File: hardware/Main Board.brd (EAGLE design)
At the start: 57.1 x 76.2 mm, 52 parts, among them Q1 CSD87313DMS, Q2 CSD16406Q3, U1 BQ24210, U2 BQ29733DSER, U3 LP38693MPX-ADJ/NOPB, U4 ESP-WROOM-02D, U5 INA219AID, U6 TC78H630FNG/TSSOP16, U7 LT1716

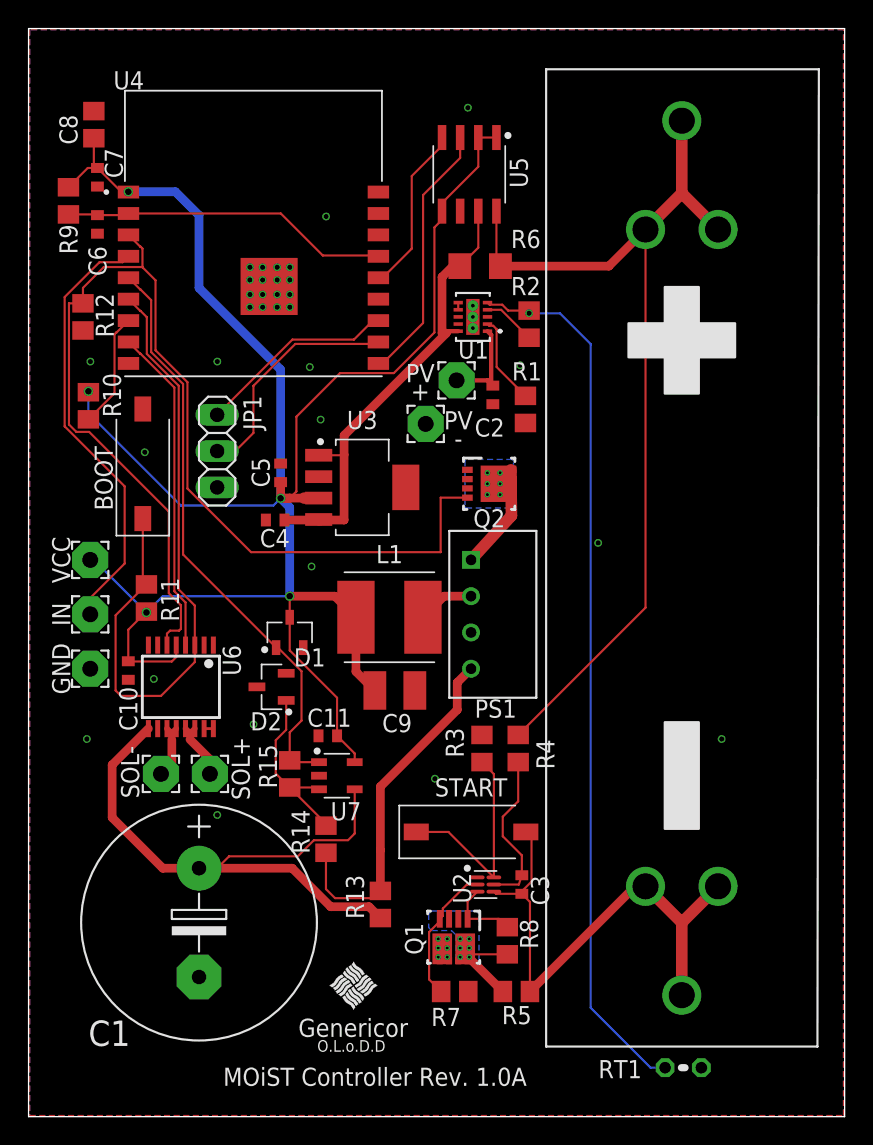
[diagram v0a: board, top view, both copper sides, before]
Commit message: Update docs for Rev 1.1B changes
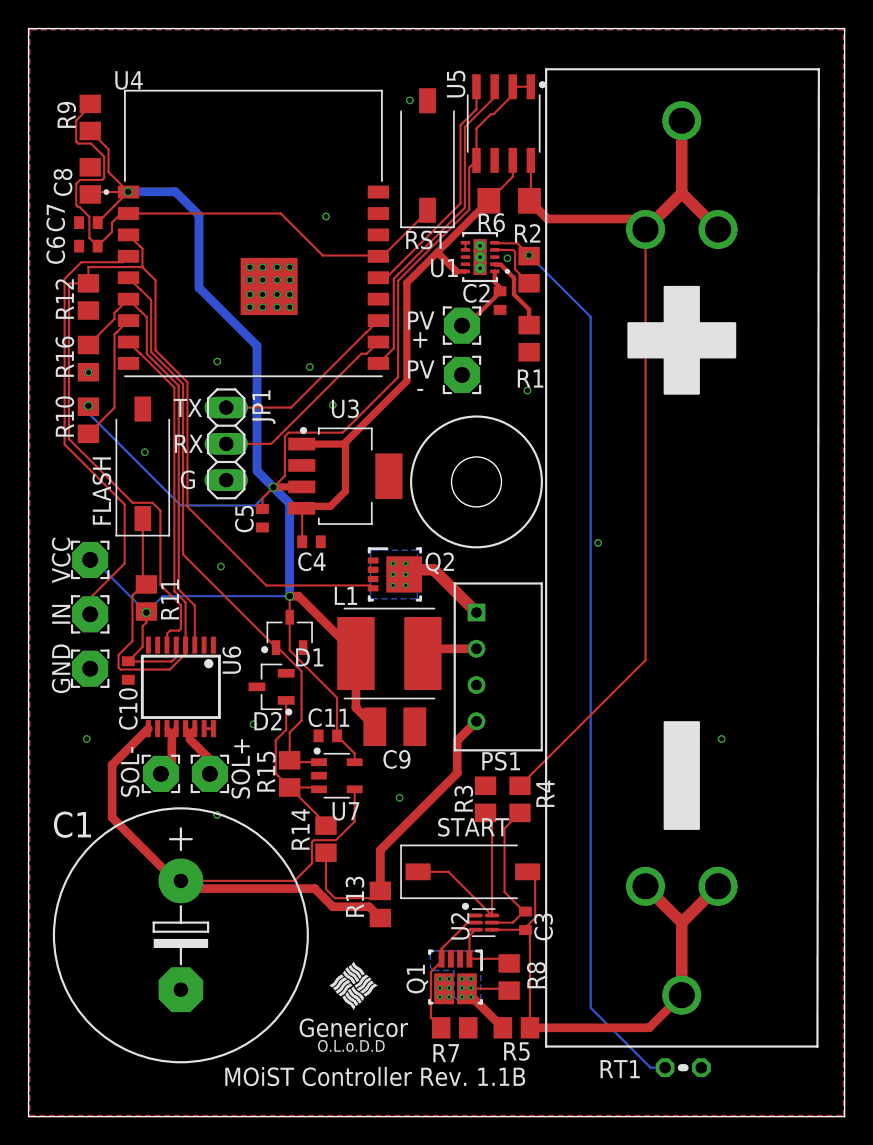
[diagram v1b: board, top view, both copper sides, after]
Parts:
- added R16: 10KΩ, rcl:R0805
- added RST: PTS636_SL43_SMTR_LFS, Genericor Parts:S_43
- C1: device rcl:E7,5-16 -> Genericor Parts:E7,5-18
- moved Q2 9.16 mm to (25.7, 38.0)
- moved C2 6.62 mm to (33.0, 57.1)
- moved R9 6.04 mm to (4.32, 70.0), turned to 90 degrees
- moved R6 5.00 mm to (33.7, 64.1)
- moved R1 4.96 mm to (35.1, 54.5)
- moved U5 4.30 mm to (33.3, 69.5)
- moved JP3 4.27 mm to (30.4, 51.9)
- moved U1 4.22 mm to (31.6, 60.2)
- moved C8 3.95 mm to (4.32, 65.5)
- moved JP2 3.85 mm to (30.4, 55.4)
- moved R2 3.81 mm to (35.1, 59.3)
- moved PS1 3.70 mm to (31.4, 35.3)
- moved R3 3.57 mm to (32.0, 22.2)
- moved R4 3.56 mm to (34.4, 22.2)
- moved C5 3.42 mm to (16.4, 41.9), turned to 270 degrees
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- renumbered BOOT to FLASH
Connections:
- net DRV_1: now also FLASH.C, R11.2
- net DRV_2: now also R16.1; no longer FLASH.C, R11.2
- net EN-RST: now also RST.C
- net GND: now also R16.2, RST.A
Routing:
- net EN-RST: track 23.0 -> 41.2 mm
- net DRV_1: track 22.9 -> 40.2 mm
- net DRV_2: track 47.1 -> 30.6 mm
- net DRV_EN: track 80.1 -> 72.6 mm
- net +3V3: track 149.5 -> 156.6 mm
- net VBATT: track 33.1 -> 39.5 mm
- net SCL: track 11.8 -> 16.5 mm
- net SDA: track 18.4 -> 22.8 mm
- net 9V+: track 25.0 -> 21.5 mm
- net RXD: track 16.4 -> 13.6 mm
- net TS: track 62.0 -> 64.5 mm
- net VM: track 44.0 -> 46.0 mm
- net Q1S1: track 8.10 -> 9.81 mm
- net PV+: track 6.66 -> 5.25 mm
- net V-: track 15.2 -> 13.8 mm
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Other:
- board text added: "MOiST Controller Rev. 1.1B"
- board text added: "TX RX G"
- board text removed: "MOiST Controller Rev. 1.0A"
